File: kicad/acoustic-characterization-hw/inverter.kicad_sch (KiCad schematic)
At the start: 0 parts

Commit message: [simulations] Updated sim with new values [kicad] Added inverter circuitry to schematic, add bulk capacitor LCSC parts, add pads for power connections.
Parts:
- added C1, C2, C9: 230nF, symbol Device:C_Small
- added C10, C11, C12, C6, C8: 10nF, Capacitor_SMD:C_0402_1005Metric, symbol Device:C_Small
- added C3, C4: 1uF, Capacitor_SMD:C_1206_3216Metric, symbol Device:C_Small
- added C5, C7: 300uF, symbol Device:C_Small
- added Q1, Q2, Q3, Q4: SI7454FDP-T1-RE3, Package_SO:PowerPAK_SO-8_Single, symbol Transistor_FET:Si7450DP
- added R1, R2, R3, R4: 10, Resistor_SMD:R_1206_3216Metric, symbol Device:R_Small
- added R10, R5, R6, R7, R8, R9: 1, Capacitor_SMD:C_0603_1608Metric, symbol Device:R_Small
- added U1, U2: UCC27282DR, symbol ucc27282:UCC27282DR
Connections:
- new net: Q1.4 (G), R3.1
- new net: C8.2, R5.1
- new net: Q2.4 (G), R4.1
- new net: R4.2, U2.8 (LO)
- new net: C10.2, R7.1
- new net: C6.2, R9.1
- new net: C11.2, R8.1
- new net: Q4.4 (G), R2.1
- new net: R2.2, U1.8 (LO)
- new net: C2.1, U1.2 (HB)
- new net: R1.2, U1.3 (HO)
- new net: C1.1, U2.2 (HB)
- new net: R3.2, U2.3 (HO)
- new net: C9.1, R6.1
- new net: C12.2, R10.1
- new net: Q3.4 (G), R1.1
- new net +12V: C3.1, C4.1, U1.1 (VDD), U2.1 (VDD)
- new net +BATT: C5.1, C7.1, Q1.5 (D), Q3.5 (D), R10.2, R7.2
- new net GND: C10.1, C11.1, C12.1, C3.2, C4.2, C5.2, C6.1, C7.2, C8.1, C9.2, Q2.1 (S), Q2.2 (S), Q2.3 (S), Q4.1 (S), Q4.2 (S), Q4.3 (S), R6.2, R8.2, U1.7 (VSS), U2.7 (VSS)
- new net INV_PWM0_HI: U1.5 (HI)
- new net INV_PWM0_LI: U1.6 (LI)
- new net INV_PWM0_LOAD: C2.2, Q3.1 (S), Q3.2 (S), Q3.3 (S), Q4.5 (D), R9.2, U1.4 (HS)
- new net INV_PWM1_HI: U2.5 (HI)
- new net INV_PWM1_LI: U2.6 (LI)
- new net INV_PWM1_LOAD: C1.2, Q1.1 (S), Q1.2 (S), Q1.3 (S), Q2.5 (D), R5.2, U2.4 (HS)
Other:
- note added: "Notes: - Make sure to correctly connect the bootstrap circuit (Hs to phase voltage) - Make sure to connect all 4 PWM inputs to different PWM drivers => ENSURE DEAD TIME WHEN DRIVING"

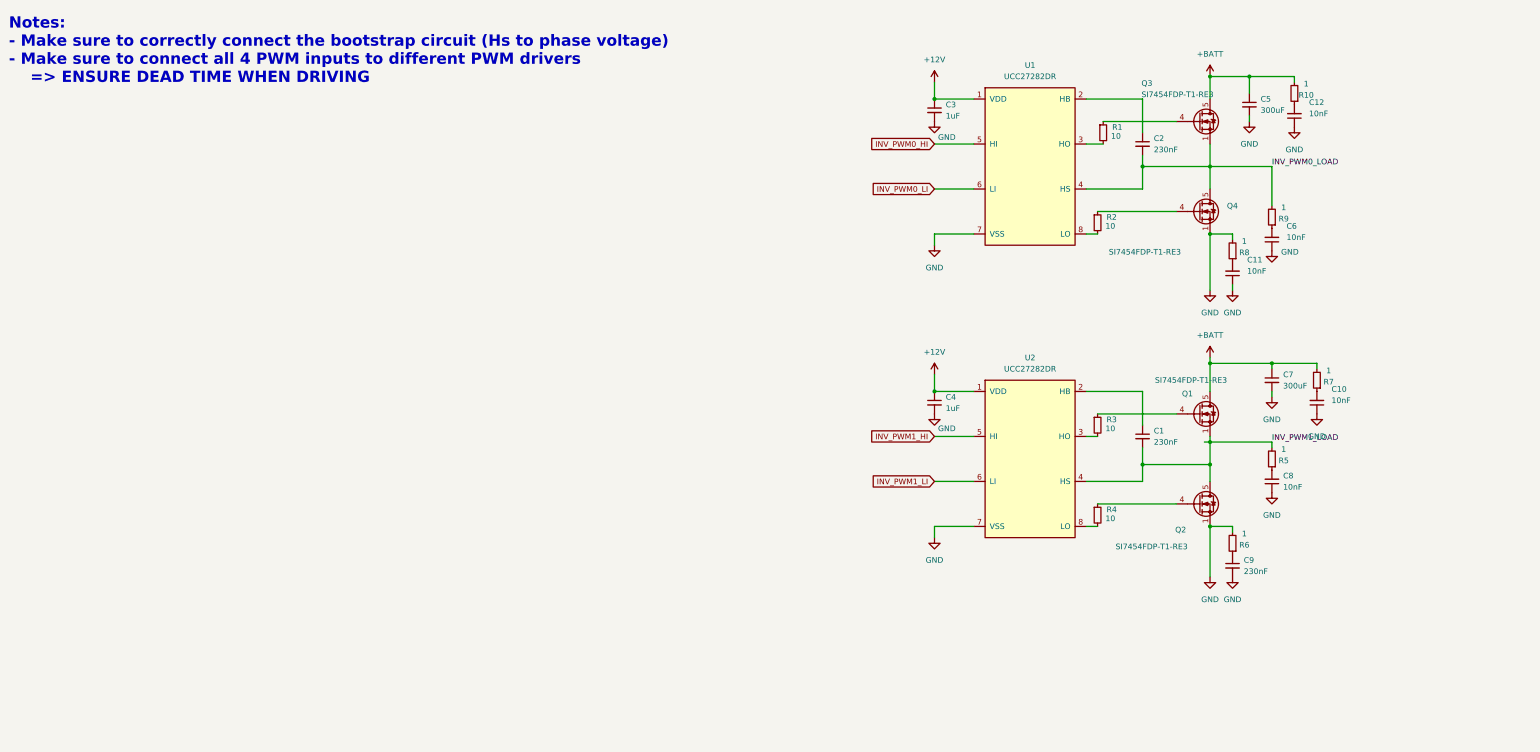
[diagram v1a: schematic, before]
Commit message: [kicad] Added capacitors, [documentation] Added bootstrap + HF frequency capacitor calculations
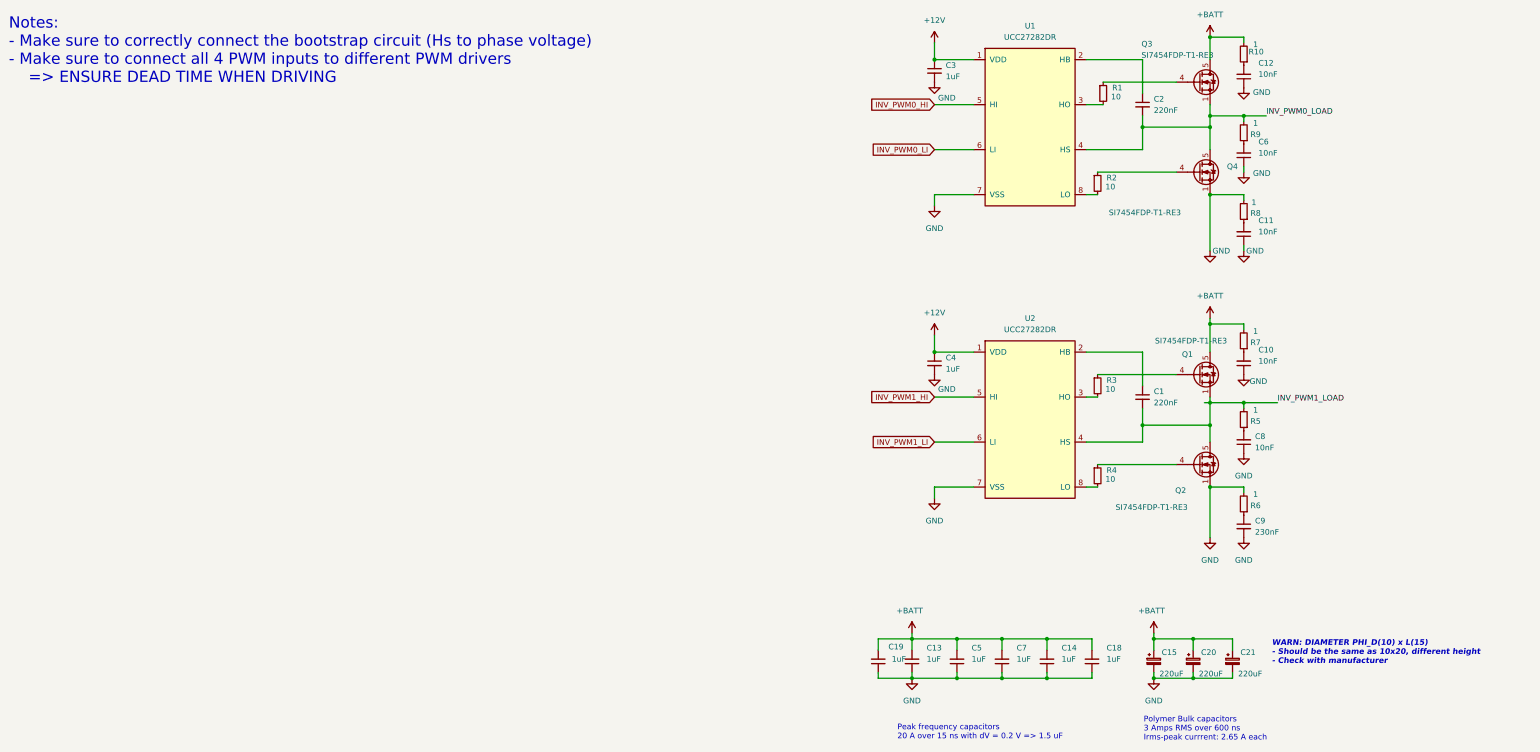
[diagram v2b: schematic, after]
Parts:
- added C13, C14, C18, C19: 1uF, Capacitor_SMD:C_0805_2012Metric, symbol Device:C_Small
- added C15, C20, C21: 220uF, Capacitor_THT:C_Radial_D10.0mm_H16.0mm_P5.00mm, symbol Device:C_Polarized_Small
- C1, C2: value 230nF -> 220nF; footprint (none) -> Capacitor_SMD:C_0805_2012Metric; LCSC Part Number (none) -> C5378; Manufacturing Part Number (none) -> CL21B224KBFNNNE
- C5, C7: value 300uF -> 1uF; footprint (none) -> Capacitor_SMD:C_0805_2012Metric; LCSC Part Number (none) -> C28323; Manufacturing Part Number (none) -> CL21B105KBFNNNE
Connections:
- net +BATT: now also C5.2, C7.2, C13.2, C14.2, C15.1, C18.2, C19.2, C20.1, C21.1; no longer C5.1, C7.1
- net GND: now also C5.1, C7.1, C13.1, C14.1, C15.2, C18.1, C19.1, C20.2, C21.2; no longer C5.2, C7.2
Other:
- note added: "Peak frequency capacitors 20 A over 15 ns with dV = 0.2 V => 1.5 uF"
- note added: "Polymer Bulk capacitors 3 Amps RMS over 600 ns Irms-peak currrent: 2.65 A each"
- note added: "WARN: DIAMETER PHI_D(10) x L(15) - Should be the same as 10x20, different height - Check with manufacturer"
- moved on the sheet: C10, C11, C12, C2, C3, C4, C6, C8, C9, Q1, Q2, Q3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

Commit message: [documentation, kicad] Added decoupling capacitors + input circuitry for adc (next) Look for a decent connector
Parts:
- C3, C4: footprint Capacitor_SMD:C_1206_3216Metric -> Capacitor_SMD:C_0805_2012Metric; LCSC Part Number C1848 -> C28323; Manufacturing Part Number CL31B105KBHNNNE -> CL21B105KBFNNNE
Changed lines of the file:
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@@
 	)
 	(junction
-		(at 29.21 95.25)
-		(diameter 0)
-		(color 0 0 0 0)
-	)
-	(junction
 		(at 44.45 168.91)
 		(diameter 0)
@@
 	)
 	(junction
+		(at 29.21 95.25)
+		(diameter 0)
+		(color 0 0 0 0)
+	)
+	(junction
 		(at 44.45 160.02)
 		(diameter 0)
@@
 	)
 	(symbol
+		(lib_id "Device:C_Small")
+		(at 29.21 97.79 0)
+		(unit 1)
+		(exclude_from_sim no)
+		(in_bom yes)
+		(on_board yes)
+		(dnp no)
+		(fields_autoplaced yes)
+		(property "Reference" "C4"
+			(at 31.75 96.5262 0)
+			(effects
+				(font
+					(size 1.27 1.27)
+				)
+				(justify left)
+			)
+		)
+		(property "Value" "1uF"
+			(at 31.75 99.0662 0)
+			(effects
+				(font
+					(size 1.27 1.27)
+				)
+				(justify left)
+			)
+		)
+		(property "Footprint" "Capacitor_SMD:C_0805_2012Metric"
+			(at 29.21 97.79 0)
+			(effects
+				(font
+					(size 1.27 1.27)
+				)
+				(hide yes)
+			)
+		)
+		(property "Datasheet" "https://jlcpcb.com/api/file/downloadByFileSystemAccessId/8579706862004473856"
+			(at 29.21 97.79 0)
+			(effects
+				(font
+					(size 1.27 1.27)
+				)
+				(hide yes)
+			)
+		)
+		(property "Description" "Unpolarized capacitor, small symbol"
+			(at 29.21 97.79 0)
+			(effects
+				(font
+					(size 1.27 1.27)
+				)
+				(hide yes)
+			)
+		)
+		(property "Manufacturing Part Number" "CL21B105KBFNNNE"
+			(at 29.21 97.79 0)
+			(effects
+				(font
+					(size 1.27 1.27)
+				)
+				(hide yes)
+			)
+		)
+		(property "LCSC Part Number" "C28323"
+			(at 29.21 97.79 0)
+			(effects
+				(font
+					(size 1.27 1.27)
+				)
+				(hide yes)
+			)
+		)
+		(pin "1"
+		)
+		(pin "2"
+		)
+		(instances
+			(project "acoustic-characterization-hw"
+				(path "/25b015c9-ab13-4427-b72c-b6f348597100/5e6fba8e-e7e0-45ab-a830-fc281a3b250c"
+					(reference "C4")
+					(unit 1)
+				)
+			)
+		)
+	)
+	(symbol
 		(lib_id "Transistor_FET:Si7450DP")
 		(at 88.9 100.33 0)
@@
 	)
 	(symbol
-		(lib_id "Device:C_Small")
-		(at 29.21 97.79 0)
-		(unit 1)
-		(exclude_from_sim no)
-		(in_bom yes)
-		(on_board yes)
-		(dnp no)
-		(fields_autoplaced yes)
-		(property "Reference" "C4"
-			(at 31.75 96.5262 0)
-			(effects
-				(font
-					(size 1.27 1.27)
-				)
-				(justify left)
-			)
-		)
-		(property "Value" "1uF"
-			(at 31.75 99.0662 0)
-			(effects
-				(font
-					(size 1.27 1.27)
-				)
-				(justify left)
-			)
-		)
-		(property "Footprint" "Capacitor_SMD:C_1206_3216Metric"
-			(at 29.21 97.79 0)
-			(effects
-				(font
-					(size 1.27 1.27)
-				)
-				(hide yes)
-			)
-		)
-		(property "Datasheet" "https://wmsc.lcsc.com/wmsc/upload/file/pdf/v2/lcsc/2304140030_Samsung-Electro-Mechanics-CL31B105KBHNNNE_C1848.pdf"
-			(at 29.21 97.79 0)
-			(effects
-				(font
-					(size 1.27 1.27)
-				)
-				(hide yes)
-			)
-		)
-		(property "Description" "Unpolarized capacitor, small symbol"
-			(at 29.21 97.79 0)
-			(effects
-				(font
-					(size 1.27 1.27)
-				)
-				(hide yes)
-			)
-		)
-		(property "Manufacturing Part Number" "CL31B105KBHNNNE"
-			(at 29.21 97.79 0)
-			(effects
-				(font
-					(size 1.27 1.27)
-				)
-				(hide yes)
-			)
-		)
-		(property "LCSC Part Number" "C1848"
-			(at 29.21 97.79 0)
-			(effects
-				(font
-					(size 1.27 1.27)
-				)
-				(hide yes)
-			)
-		)
-		(pin "1"
-		)
-		(pin "2"
-		)
-		(instances
-			(project "acoustic-characterization-hw"
-				(path "/25b015c9-ab13-4427-b72c-b6f348597100/5e6fba8e-e7e0-45ab-a830-fc281a3b250c"
-					(reference "C4")
-					(unit 1)
-				)
-			)
-		)
-	)
-	(symbol
 		(lib_id "power:+BATT")
 		(at 78.74 158.75 0)
@@
 			)
 		)
-		(property "Footprint" "Capacitor_SMD:C_1206_3216Metric"
+		(property "Footprint" "Capacitor_SMD:C_0805_2012Metric"
 			(at 29.21 31.75 0)
 			(effects
@@
 			)
 		)
-		(property "Datasheet" "https://wmsc.lcsc.com/wmsc/upload/file/pdf/v2/lcsc/2304140030_Samsung-Electro-Mechanics-CL31B105KBHNNNE_C1848.pdf"
+		(property "Datasheet" "https://jlcpcb.com/api/file/downloadByFileSystemAccessId/8579706862004473856"
 			(at 29.21 31.75 0)
 			(effects
@@
 			)
 		)
-		(property "Manufacturing Part Number" "CL31B105KBHNNNE"
+		(property "Manufacturing Part Number" "CL21B105KBFNNNE"
 			(at 29.21 31.75 0)
 			(effects
@@
 			)
 		)
-		(property "LCSC Part Number" "C1848"
+		(property "LCSC Part Number" "C28323"
 			(at 29.21 31.75 0)
 			(effects

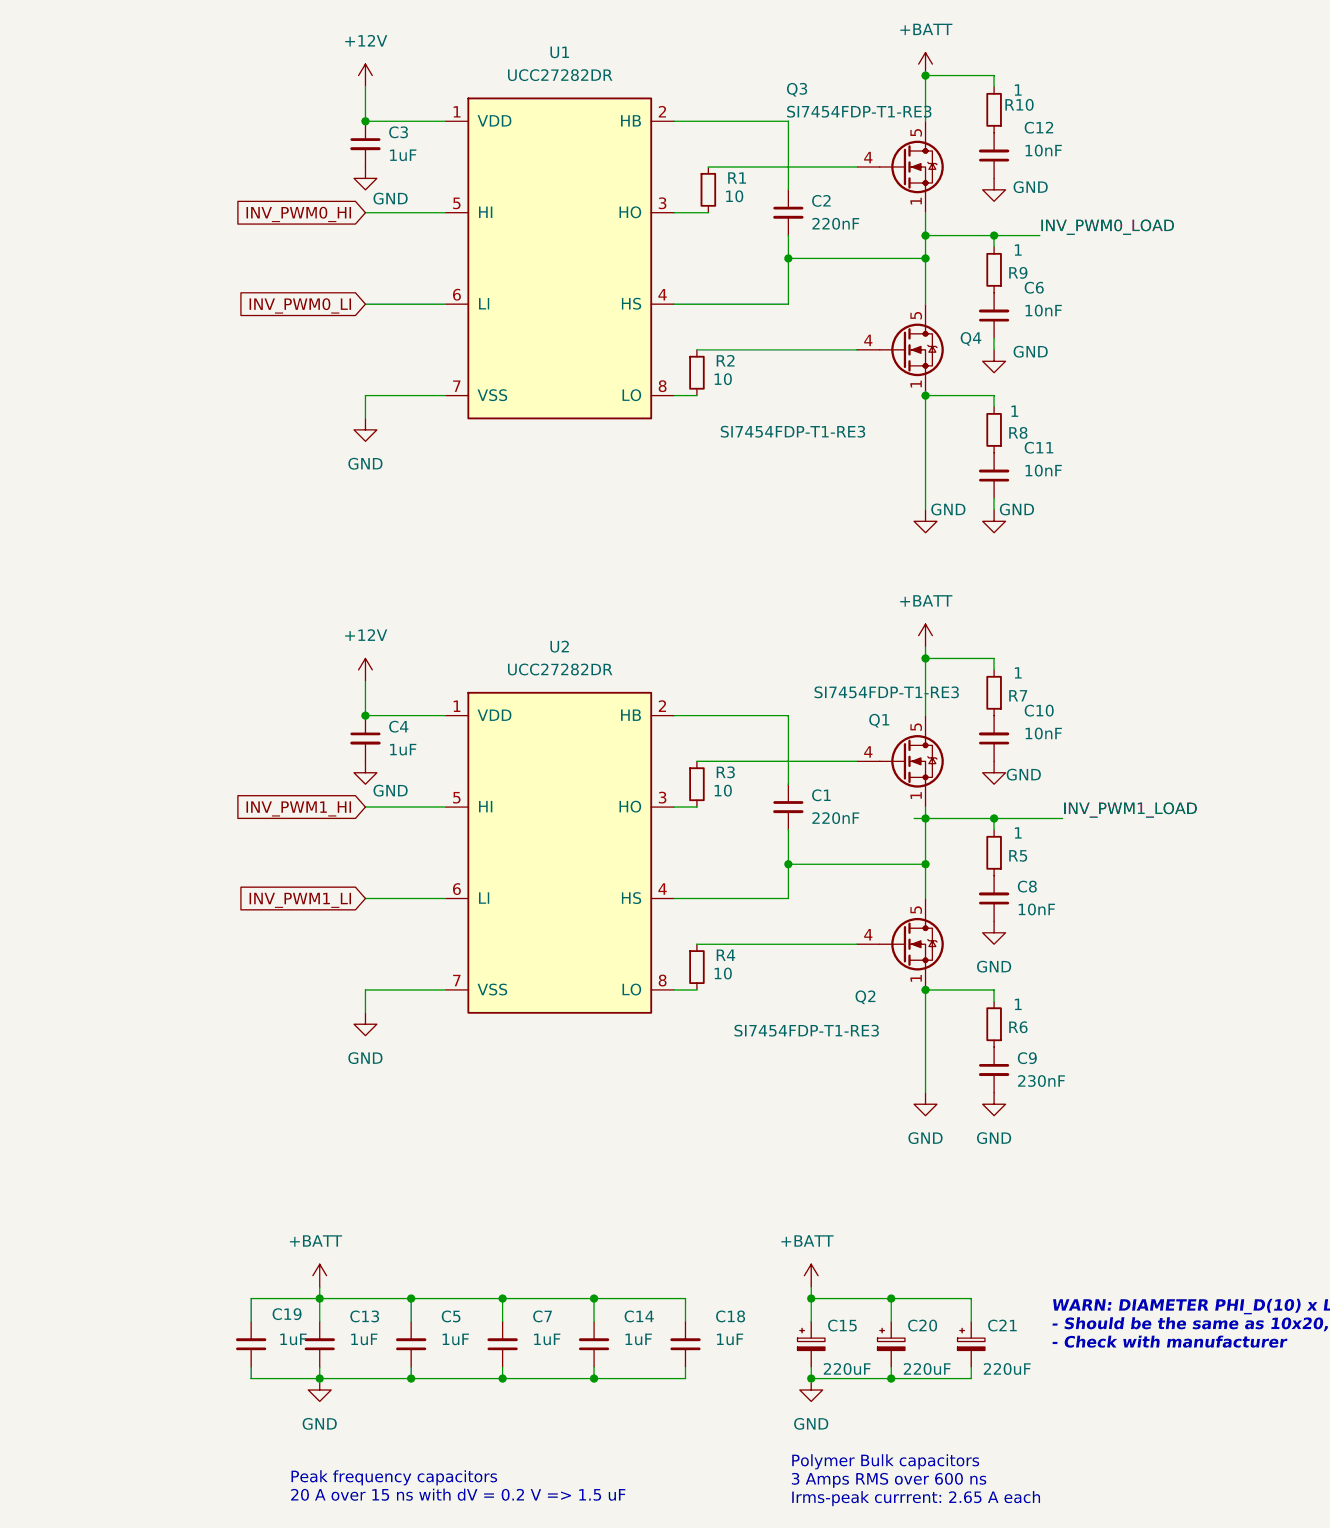
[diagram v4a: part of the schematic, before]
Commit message: [kicad] Connected DDR3L bus, added info on FPGA and ddr pin functionality (next) add filtering circuitry for DDR power pins
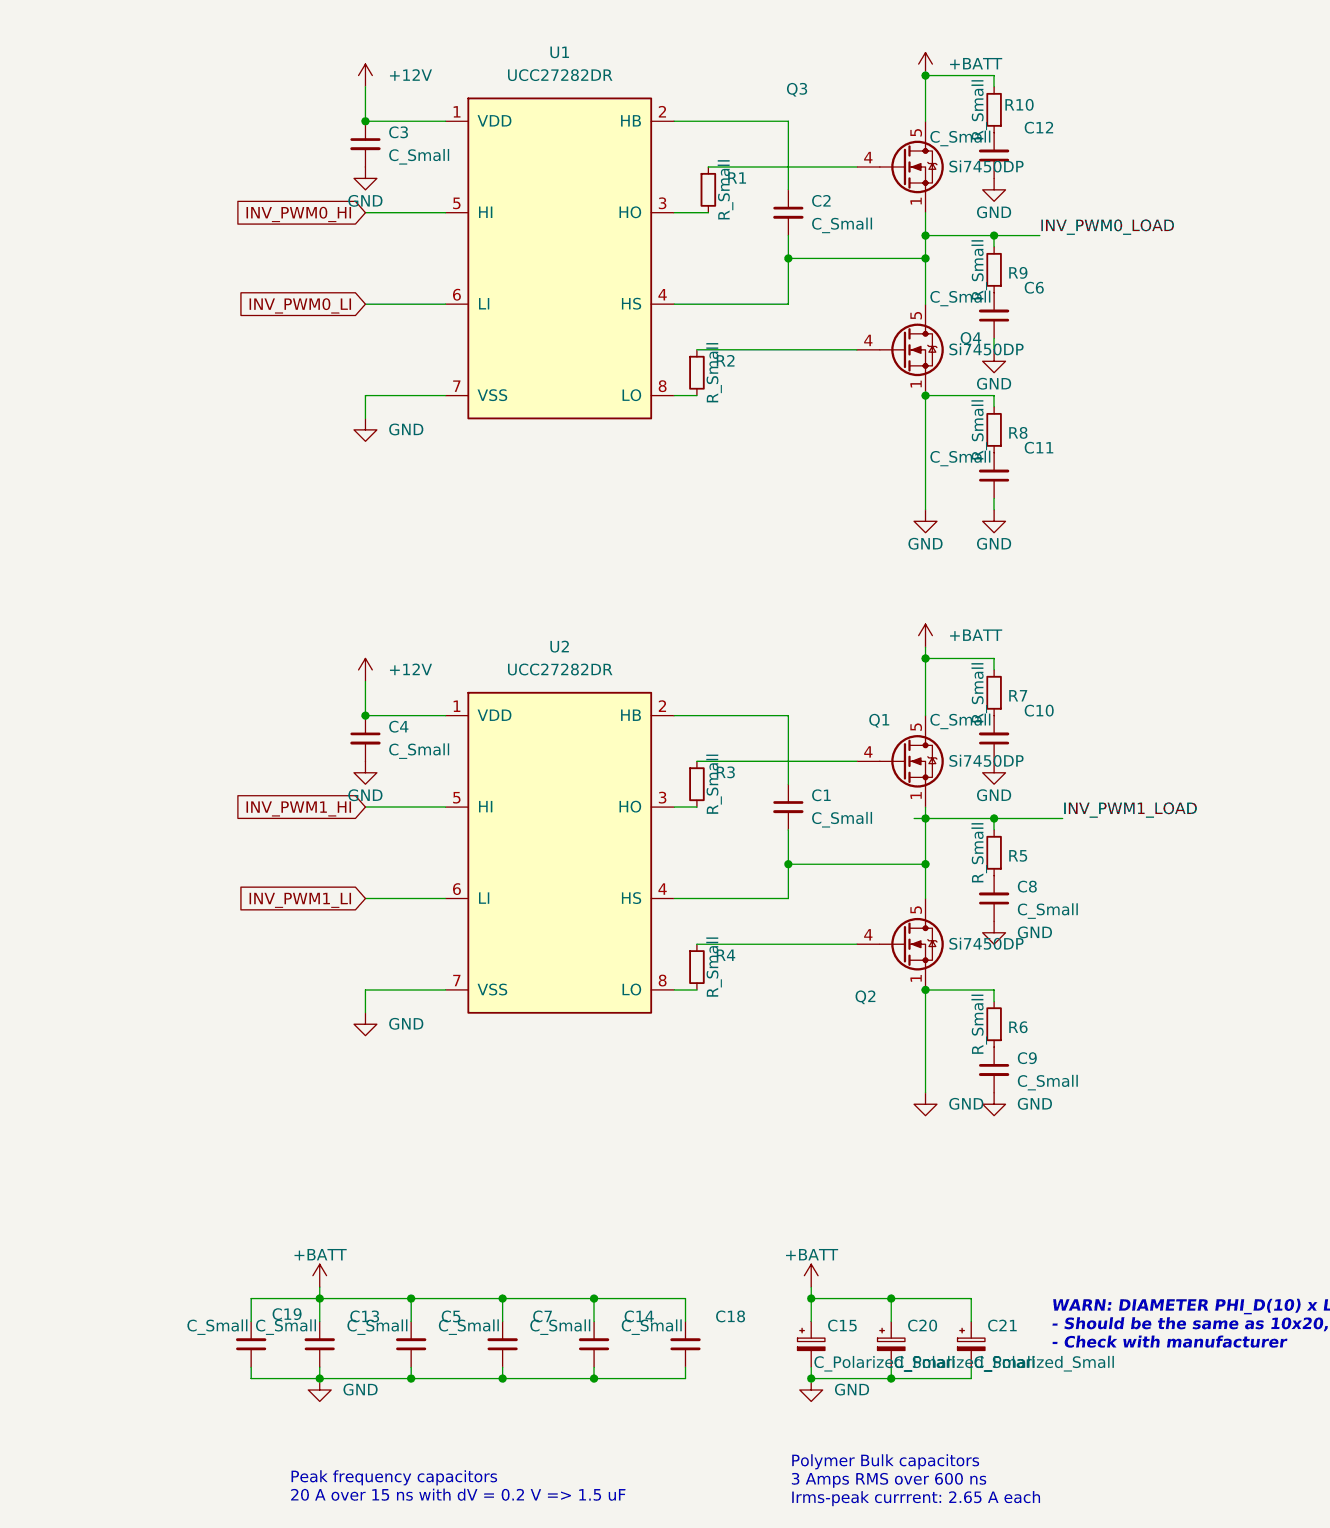
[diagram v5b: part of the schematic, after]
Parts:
- C1, C2: value 220nF -> C_Small
- C10, C11, C12, C6, C8: value 10nF -> C_Small
- C13, C14, C18, C19, C3, C4, C5, C7: value 1uF -> C_Small
- C15, C20, C21: value 220uF -> C_Polarized_Small
- C9: value 230nF -> C_Small
- Q1, Q2, Q3, Q4: value SI7454FDP-T1-RE3 -> Si7450DP
- R1, R2, R3, R4: value 10 -> R_Small
- R10, R5, R6, R7, R8, R9: value 1 -> R_Small
